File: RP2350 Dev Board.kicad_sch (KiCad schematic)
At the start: 48 parts, among them U2 SM03B-SRSS-TB(LF)(SN)(P), U4 W25Q128

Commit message: Re-did schematic
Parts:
- removed R1, R4: 5.1kΩ, RP2350 Dev Board:, symbol ProPrj_RP2-easyedapro:0402WGJ0512TCE
- removed R11: 100kΩ, RP2350 Dev Board:R0402, symbol ProPrj_RP2-easyedapro:RC0402FR-07100KL
- removed R12: 2kΩ, RP2350 Dev Board:R0402, symbol ProPrj_RP2-easyedapro:0402WGF2001TCE
- removed R2, R3: 33Ω, RP2350 Dev Board:, symbol ProPrj_RP2-easyedapro:0402WGF270JTCE
- removed R28: 1kΩ, RP2350 Dev Board:, symbol ProPrj_RP2-easyedapro:0402WGF1001TCE
- removed R5: 1kΩ, RP2350 Dev Board:R0402, symbol ProPrj_RP2-easyedapro:0402WGJ0102TCE
- added J1, J2: Conn_01x30_MountingPin, symbol Connector_Generic_MountingPin:Conn_01x30_MountingPin
- added R1, R4: 5.1kΩ, PCM_JLCPCB:R_0402, symbol PCM_JLCPCB-Resistors:0402,5.1kΩ
- added R11: 100kΩ, PCM_JLCPCB:R_0402, symbol PCM_JLCPCB-Resistors:0402,100kΩ
- added R12: 2kΩ, PCM_JLCPCB:R_0402, symbol PCM_JLCPCB-Resistors:0402,2kΩ
- added R2, R3: 33Ω, PCM_JLCPCB:R_0402, symbol PCM_JLCPCB-Resistors:0402,33Ω
- added R28: 1kΩ, PCM_JLCPCB:R_0603, symbol PCM_JLCPCB-Resistors:0603,1kΩ
- added R5: 1kΩ, PCM_JLCPCB:R_0402, symbol PCM_JLCPCB-Resistors:0402,1kΩ
- Boot1: footprint RP2350 Dev Board:KEY-SMD_4P-L4.2-W3.2-P2.20-LS5.1-TL -> EasyEDA:KEY-SMD_4P-L4.2-W3.2-P2.20-LS5.1-TL; symbol ProPrj_RP2-easyedapro:K2-1808SN-A4SW -> EasyEDA:K2-1808SN-A4SW; LCSC Part (none) -> C92589
- C17, C18: footprint RP2350 Dev Board: -> EasyEDA:C0402; symbol ProPrj_RP2-easyedapro:GRM1555C1H100FA01D -> EasyEDA:0402CG150J500NT; LCSC Part (none) -> C1548
- C37, C40: footprint RP2350 Dev Board:C0402 -> EasyEDA:C0402; symbol ProPrj_RP2-easyedapro:GRM155R61A106ME44D -> EasyEDA:GRM155R61A106ME44D; LCSC Part (none) -> C77000
- C38, C39: footprint RP2350 Dev Board:C0402 -> EasyEDA:C0402; symbol ProPrj_RP2-easyedapro:GRM155R71H104KE14D -> EasyEDA:GRM155R71H104KE14D; LCSC Part (none) -> C77020
- D1: footprint RP2350 Dev Board:POWERDI-123_L2.8-W1.8-LS3.7-RD -> EasyEDA:POWERDI-123_L2.8-W1.8-LS3.7-RD; symbol ProPrj_RP2-easyedapro:DFLS130L-7 -> EasyEDA:DFLS130L-7; LCSC Part (none) -> C110493
- PWR_LED1: footprint RP2350 Dev Board:LED0402-RD -> EasyEDA:LED0402-RD; symbol ProPrj_RP2-easyedapro:FC-F1005HRK-620H5 -> EasyEDA:FC-F1005HRK-620H5; LCSC Part (none) -> C130719
- U1: footprint RP2350 Dev Board:QFN-80_L10.0-W10.0-P0.40-TL-EP3.4 -> EasyEDA:QFN-80_L10.0-W10.0-P0.40-TL-EP3.4; symbol ProPrj_RP2-easyedapro:RP2350B_C42415655 -> EasyEDA:RP2350B_C42415655; LCSC Part (none) -> C42415655
- U3: footprint RP2350 Dev Board:SOT-23-5_L3.0-W1.7-P0.95-LS2.8-BR -> EasyEDA:SOT-23-5_L3.0-W1.7-P0.95-LS2.8-BR; symbol ProPrj_RP2-easyedapro:ME6217C33M5G -> EasyEDA:ME6217C33M5G; LCSC Part (none) -> C427602
- USB1: footprint RP2350 Dev Board:USB-C-SMD_TYPE-C-6PIN-2MD-073 -> EasyEDA:USB-C-SMD_TYPE-C-6PIN-2MD-073; symbol ProPrj_RP2-easyedapro:TYPE-C 16PIN 2MD(073) -> EasyEDA:TYPE-C16PIN2MD(073); LCSC (none) -> C2765186; LCSC Part (none) -> C2765186
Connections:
- net 1V1: now also C10.2, C13.2, L2.1; no longer C10.1, C13.1, L2.2
- net 3V3: now also C12.2, C14.2, C36.2, C8.2, C9.2, J2.57 (Pin_57); no longer C12.1, C14.1, C36.1, C8.1, C9.1
- net 3V3_EN: now also J2.56 (Pin_56), R11.2
- net ADC_VREF: now also J2.55 (Pin_55)
- net GND: now also C10.1, C11.1, C12.1, C13.1, C14.1, C36.1, C8.1, C9.1, J1.11 (Pin_11), J1.22 (Pin_22), J2.39 (Pin_39), J2.50 (Pin_50), J2.54 (Pin_54), J2.58 (Pin_58), R1.1, R12.2, R4.1; no longer C10.2, C11.2, C12.2, C13.2, C14.2, C36.2, C8.2, C9.2
- net GPIO0: now also J1.1 (Pin_1)
- net GPIO1: now also J1.2 (Pin_2)
- net GPIO10: now also J1.12 (Pin_12)
- net GPIO11: now also J1.13 (Pin_13)
- net GPIO12: now also J1.14 (Pin_14)
- net GPIO13: now also J1.15 (Pin_15)
- net GPIO14: now also J1.16 (Pin_16)
- net GPIO15: now also J1.17 (Pin_17)
- net GPIO16: now also J1.18 (Pin_18)
- net GPIO17: now also J1.19 (Pin_19)
- net GPIO18: now also J1.20 (Pin_20)
- net GPIO19: now also J1.21 (Pin_21)
- net GPIO2: now also J1.3 (Pin_3)
- net GPIO20: now also J1.23 (Pin_23)
- net GPIO21: now also J1.24 (Pin_24)
- net GPIO22: now also J1.25 (Pin_25)
- net GPIO23: now also J1.26 (Pin_26)
- net GPIO24: now also J1.27 (Pin_27)
- net GPIO25: now also J1.28 (Pin_28)
- net GPIO26: now also J1.29 (Pin_29)
- net GPIO27: now also J1.30 (Pin_30)
- net GPIO28: now also J2.32 (Pin_32)
- net GPIO29: now also J2.33 (Pin_33)
- net GPIO3: now also J1.4 (Pin_4)
- net GPIO30: now also J2.34 (Pin_34)
- net GPIO31: now also J2.35 (Pin_35)
- net GPIO32: now also J2.36 (Pin_36)
- net GPIO33: now also J2.37 (Pin_37)
- net GPIO34: now also J2.38 (Pin_38)
- net GPIO35: now also J2.40 (Pin_40)
- net GPIO36: now also J2.41 (Pin_41)
- net GPIO37: now also J2.42 (Pin_42)
- net GPIO38: now also J2.43 (Pin_43)
- net GPIO39: now also J2.44 (Pin_44)
- net GPIO4: now also J1.5 (Pin_5)
- net GPIO40/ADC0: now also J2.45 (Pin_45)
- net GPIO41/ADC1: now also J2.46 (Pin_46)
- net GPIO42/ADC2: now also J2.47 (Pin_47)
- net GPIO43/ADC3: now also J2.48 (Pin_48)
- net GPIO44/ADC4: now also J2.49 (Pin_49)
- net GPIO45/ADC5: now also J2.51 (Pin_51)
- net GPIO46/ADC6: now also J2.52 (Pin_52)
- net GPIO47/ADC7: now also J2.53 (Pin_53)
- net GPIO5: now also J1.6 (Pin_6)
- net GPIO6: now also J1.7 (Pin_7)
- net GPIO7: now also J1.8 (Pin_8)
- net GPIO8: now also J1.9 (Pin_9)
- net GPIO9: now also J1.10 (Pin_10)
- net RUN: now also J2.31 (Pin_31)
- net USB2_D+: now also R3.2
- net USB2_D-: now also R2.2
- net VBUS: now also J2.60 (Pin_60)
- net VREG_LX: now also L2.2; no longer L2.1
- net VSYS: now also J2.59 (Pin_59), R11.1
- net at Boot1.1, Boot1.2: now also R5.1
- net at USB1.10 (CC2): now also R4.2
- net at USB1.4 (CC1): now also R1.2
- net at R6.2, U1.61 (VREG_AVDD): now also C11.2; no longer C11.1
- net at C17.1, X1.3: now also R28.1
- net at PWR_LED1.1 (K): now also R12.1
- net QSPI_SCLK: no longer names the net of U1.71 (QSPI_SCLK), U4.6 (CLK)
- net QSPI_SD0: no longer names the net of U1.72 (QSPI_SD0), U4.5 (DI)
- net QSPI_SD1: no longer names the net of U1.74 (QSPI_SD1), U4.2 (DO)
- net QSPI_SD2: no longer names the net of U1.73 (QSPI_SD2), U4.3 (IO2)
- net QSPI_SD3: no longer names the net of U1.70 (QSPI_SD3), U4.7 (IO3)
- net QSPI_SS: no longer names the net of U1.75 (QSPI_SS), U4.1 (CS#)
- net QSPI_SS: now also R5.2
- net SWCLK: no longer names the net of U1.33 (SWCLK), U2.1
- net SWD: no longer names the net of U1.34 (SWDIO), U2.3
- net USB_D+: no longer names the net of U1.67 (USB_DP)
- net USB_D+: now also R3.1
- net USB_D-: no longer names the net of U1.66 (USB_DM)
- net USB_D-: now also R2.1
- net XIN: no longer names the net of C18.2, U1.30 (XIN), X1.1
- net XOUT: no longer names the net of U1.31 (XOUT)
- net XOUT: now also R28.2
- no-connect marks 4 -> 6
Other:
- note added: "1V1 Power"
- note added: "Pads"
- note added: "RP2350B"
- note added: "USB Type C"
- note removed: "Core - RP2350B"
- note removed: "Type-c"
- moved on the sheet: Boot1, C1, C10, C11, C12, C13, C14, C15, C16, C17, C18, C19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

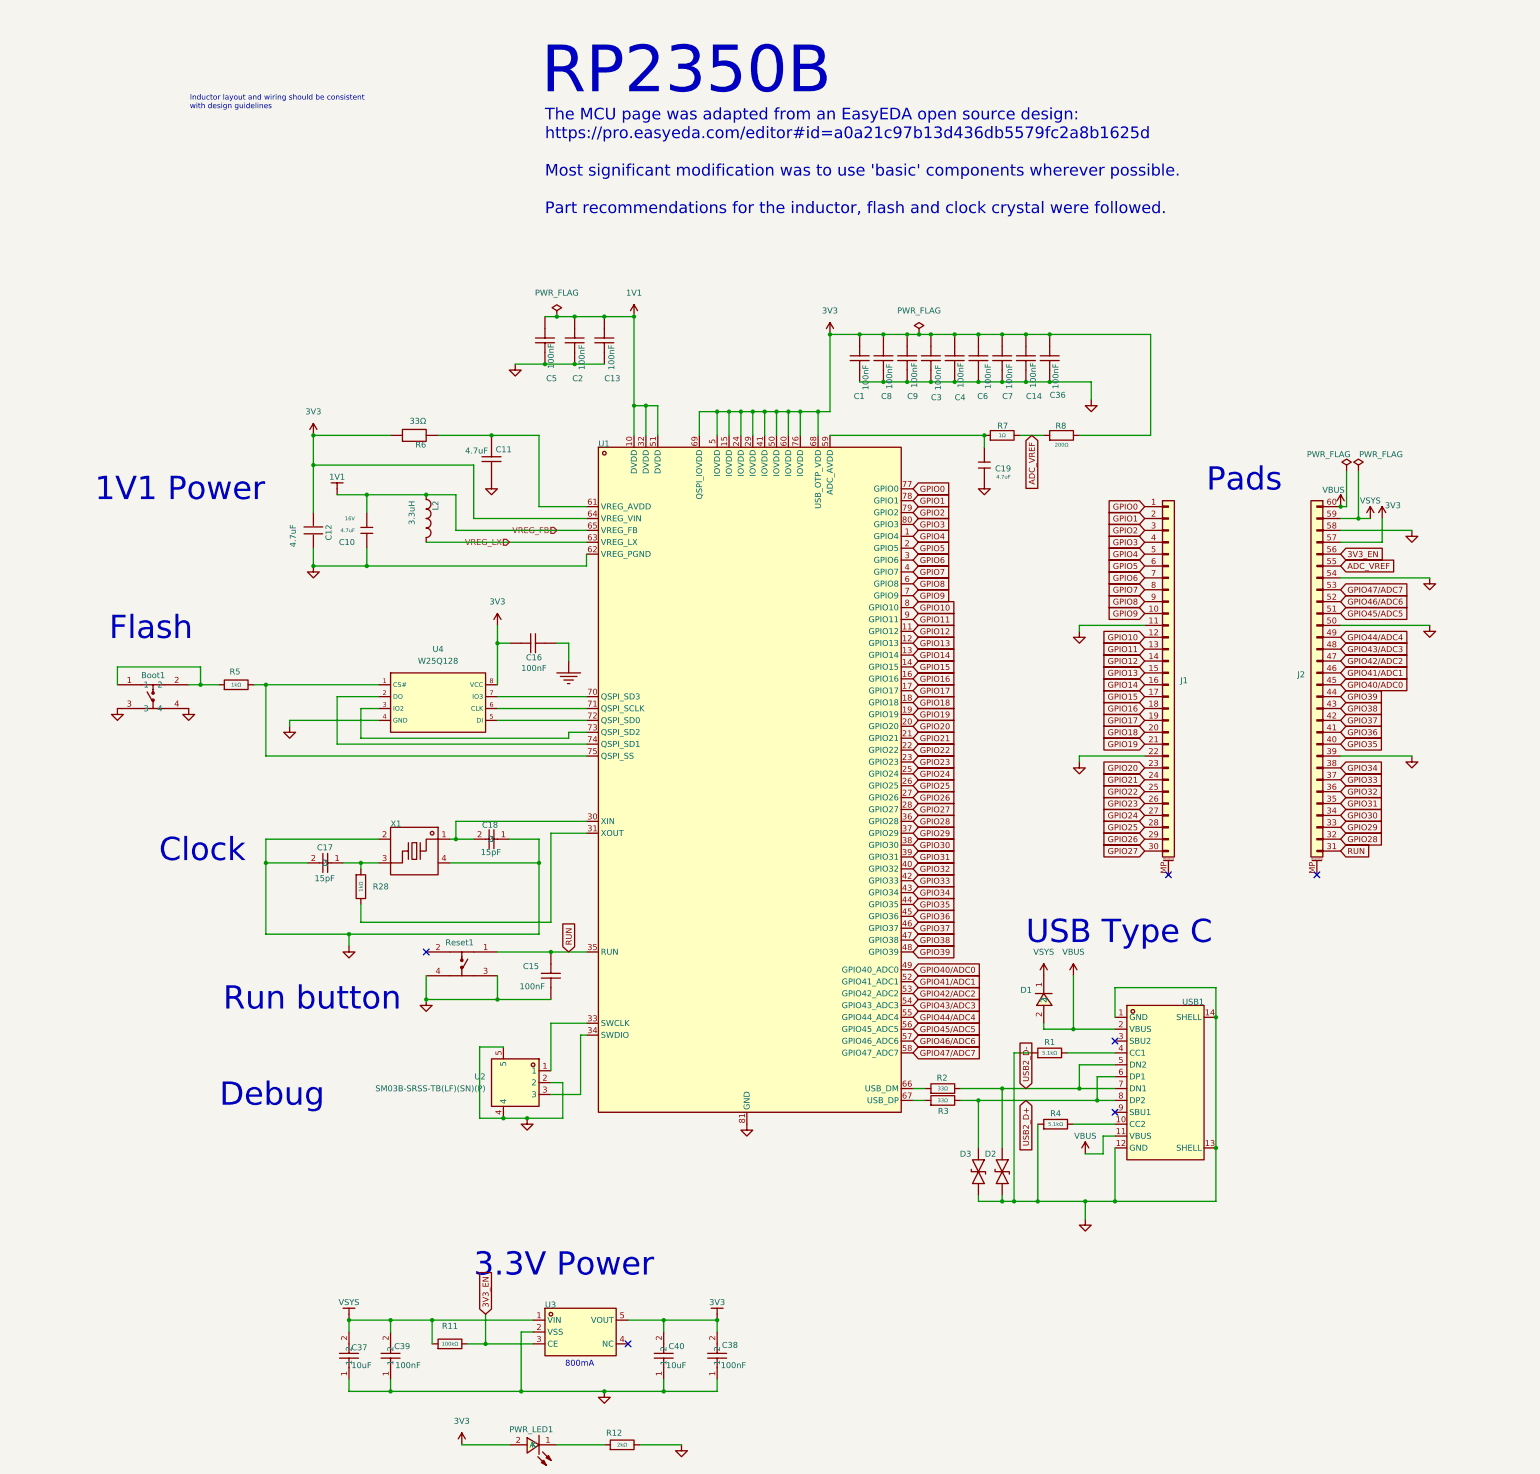
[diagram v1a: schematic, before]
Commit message: Updated footprints, more basic parts
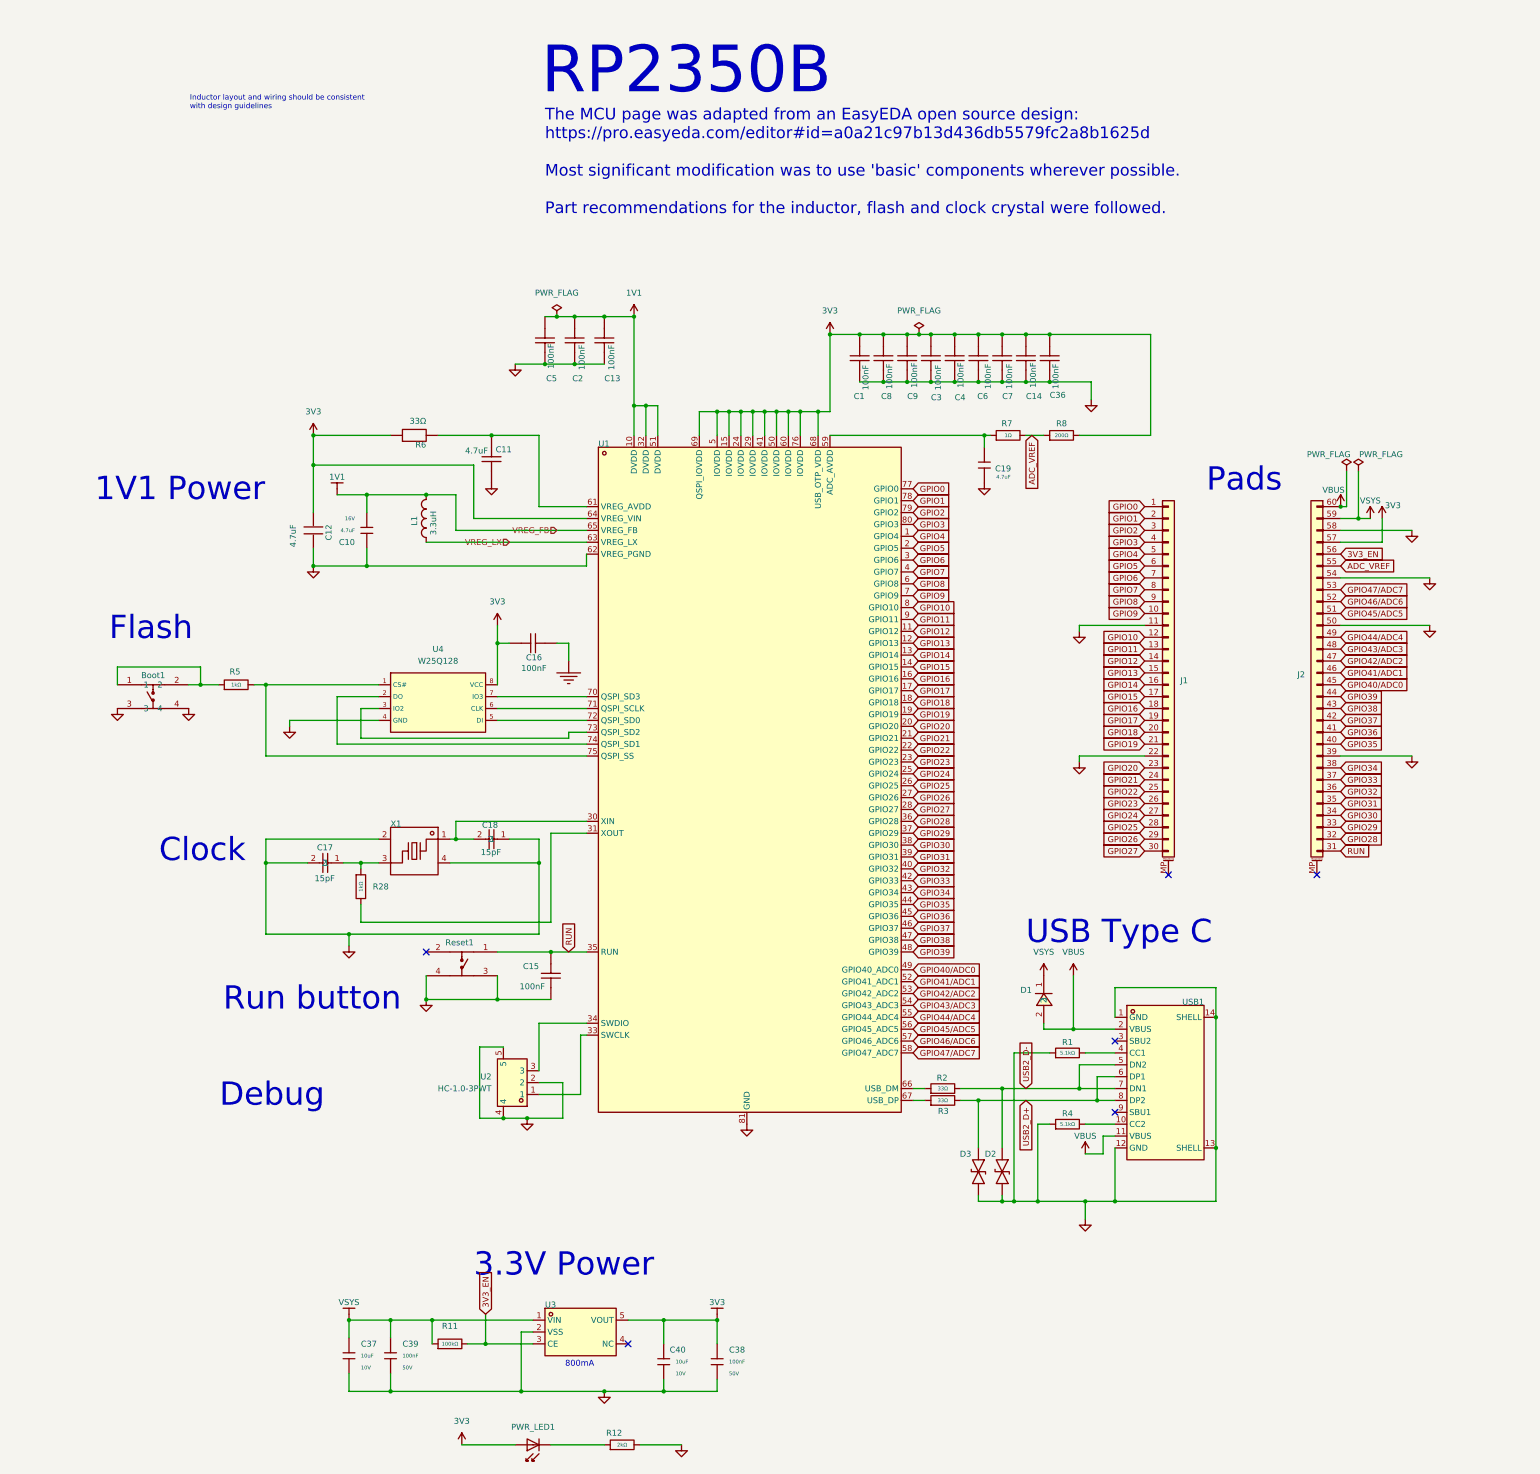
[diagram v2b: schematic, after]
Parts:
- removed C37, C40: 10uF, EasyEDA:C0402, symbol EasyEDA:GRM155R61A106ME44D
- removed C38, C39: 100nF, EasyEDA:C0402, symbol EasyEDA:GRM155R71H104KE14D
- removed PWR_LED1: ~, EasyEDA:LED0402-RD, symbol EasyEDA:FC-F1005HRK-620H5
- removed R7: 1Ω, PCM_JLCPCB:R_0402, symbol PCM_JLCPCB-Resistors:0402,1Ω
- removed R8: 200Ω, PCM_JLCPCB:R_0402, symbol PCM_JLCPCB-Resistors:0402,200Ω
- removed U2: SM03B-SRSS-TB(LF)(SN)(P), EasyEDA:CONN-SMD_SM03B-SRSS-TB-LF-SN-P, symbol Local:SM03B-SRSS-TB(LF)(SN)(P)
- added C37, C40: 10uF, PCM_JLCPCB:C_0603, symbol PCM_JLCPCB-Capacitors:0603,10uF
- added C38, C39: 100nF, PCM_JLCPCB:C_0603, symbol PCM_JLCPCB-Capacitors:0603,100nF
- added PWR_LED1: Red, PCM_JLCPCB:D_0603, symbol PCM_JLCPCB-Diodes:LED,0603,Red
- added R7: 1Ω, PCM_JLCPCB:R_0603, symbol PCM_JLCPCB-Resistors:0603,1Ω
- added R8: 200Ω, PCM_JLCPCB:R_0603, symbol PCM_JLCPCB-Resistors:0603,200Ω
- added U2: HC-1.0-3PWT, EasyEDA:CONN-SMD_3P-P1.0-HC-1.0-3PWT, symbol EasyEDA:HC-1.0-3PWT
- renumbered L2 to L1
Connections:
- net 1V1: now also L1.2; no longer L1.1
- net 3V3: now also C38.1, C40.1, PWR_LED1.2, R8.2
- net ADC_VREF: now also R7.2, R8.1
- net GND: now also C37.2, C38.2, C39.2, C40.2, U2.2, U2.4, U2.5
- net VREG_LX: now also L1.1; no longer L1.2
- net VSYS: now also C37.1, C39.1
- net at U1.33 (SWCLK): now also U2.1
- net at U1.34 (SWDIO): now also U2.3
- net at R12.1: now also PWR_LED1.1
- net at C19.1, U1.59 (ADC_AVDD): now also R7.1
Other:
- moved on the sheet: L1, R1, R4

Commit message: Added wifi and PSRAM
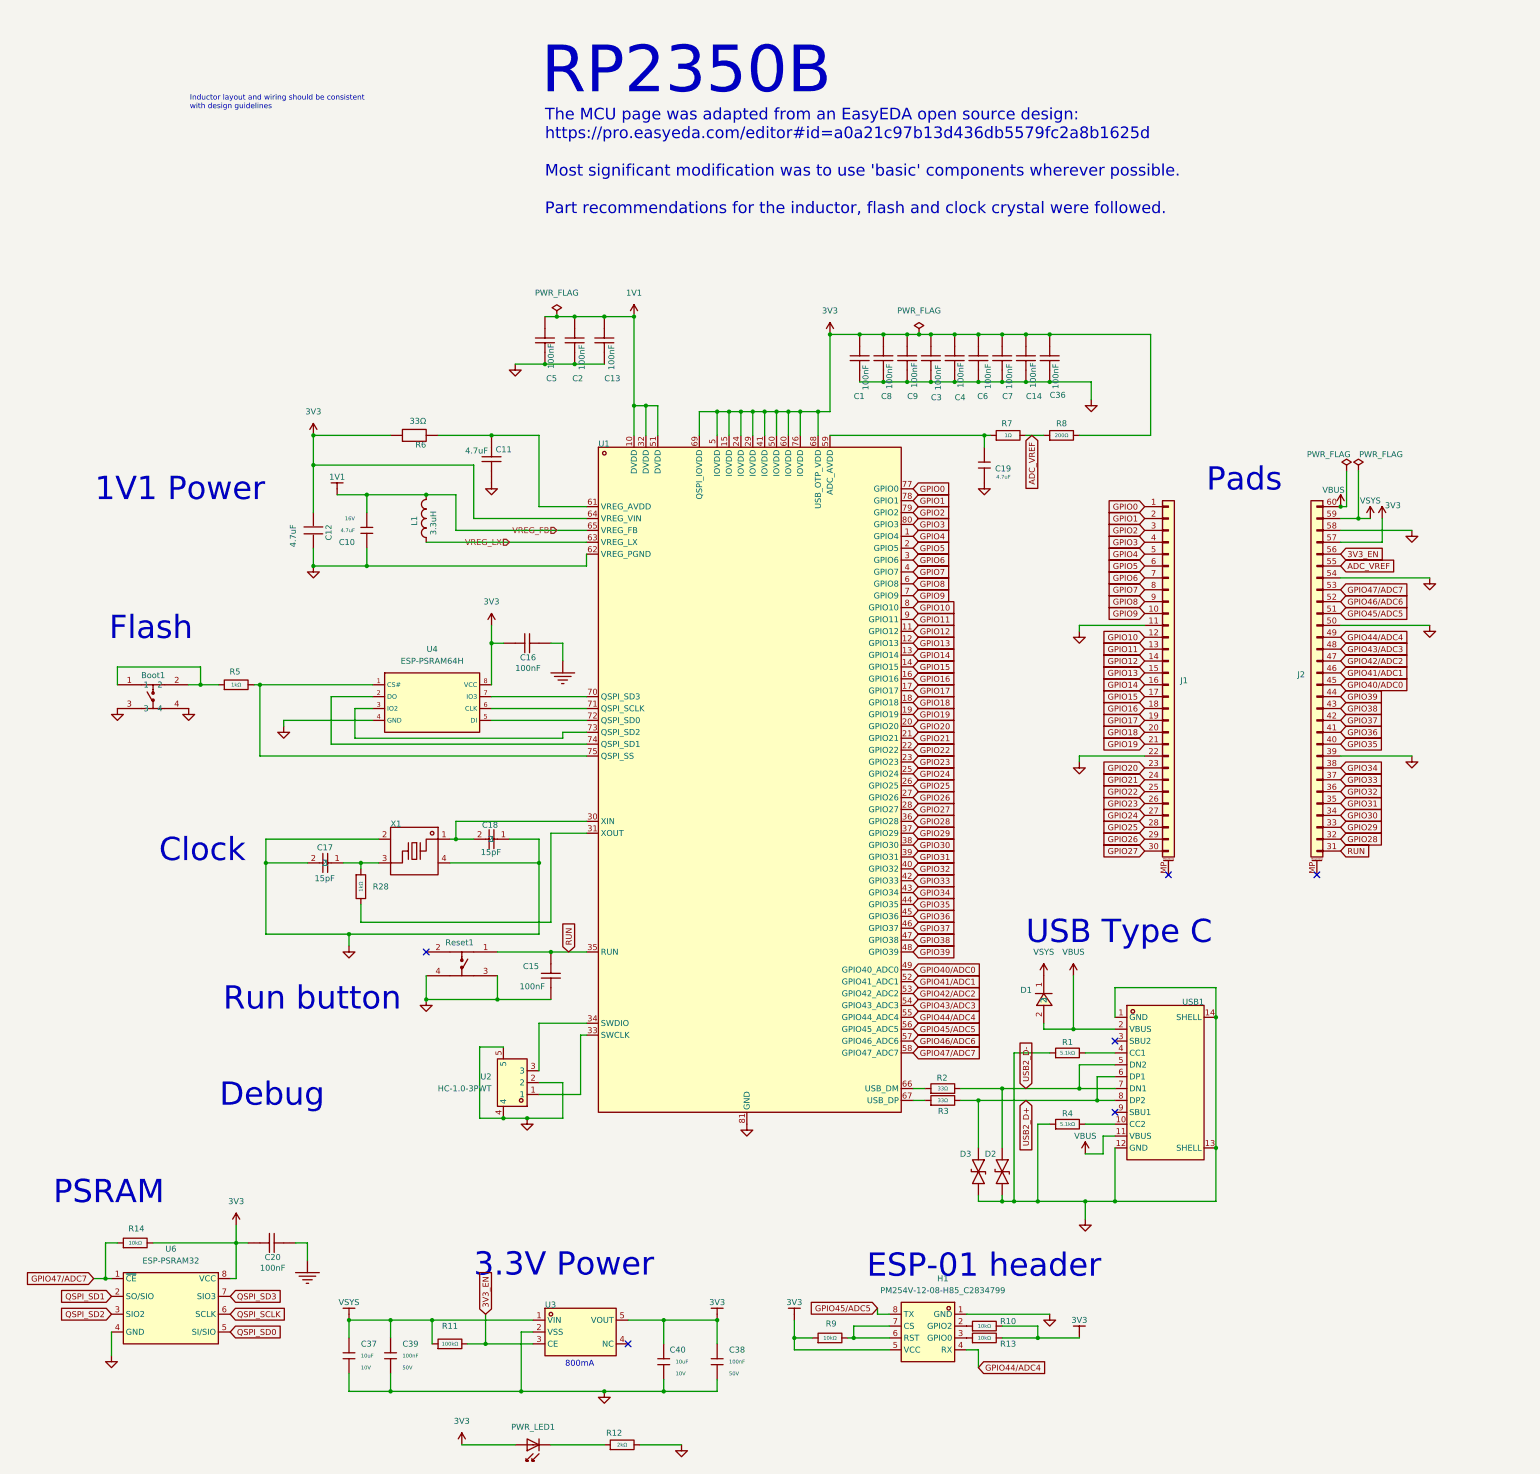
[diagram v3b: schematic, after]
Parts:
- added C20: 100nF, RP2350 Dev Board:C0402, symbol ProPrj_RP2-easyedapro:UMK105B7104KVHF
- added H1: PM254V-12-08-H85_C2834799, EasyEDA:HDR-TH_8P-P2.54-V-F-R2-C4-S2.54, symbol EasyEDA:PM254V-12-08-H85_C2834799
- added R10, R13, R14, R9: 10kΩ, PCM_JLCPCB:R_0402, symbol PCM_JLCPCB-Resistors:0402,10kΩ
- added U6: ESP-PSRAM32, Package_SO:SOIC-8_3.9x4.9mm_P1.27mm, symbol Memory_RAM:ESP-PSRAM32
- U4: value W25Q128 -> ESP-PSRAM64H
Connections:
- net 3V3: now also C20.2, H1.5 (VCC), R10.2, R13.2, R14.2, R9.1, U6.8 (VCC)
- net GND: now also C20.1, H1.1 (GND), U6.4 (GND)
- net GPIO44/ADC4: now also H1.4 (RX)
- net GPIO45/ADC5: now also H1.8 (TX)
- net GPIO47/ADC7: now also R14.1, U6.1 (~{CE})
- new net: H1.6 (RST), H1.7 (CS), R9.2
- new net: H1.2 (GPIO2), R10.1
- new net: H1.3 (GPIO0), R13.1
- new net QSPI_SCLK: U6.6 (SCLK)
- new net QSPI_SD0: U6.5 (SI/SIO)
- new net QSPI_SD1: U6.2 (SO/SIO)
- new net QSPI_SD2: U6.3 (SIO2)
- new net QSPI_SD3: U6.7 (SIO3)
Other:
- note added: "ESP-01 header"
- note added: "PSRAM"
- moved on the sheet: C16, U4
